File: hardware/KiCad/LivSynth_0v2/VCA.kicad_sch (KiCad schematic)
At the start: 24 parts, among them J18 Jumper, J6 Jumper, Q5 2N3904, Q6 2N3904, U3 TL074

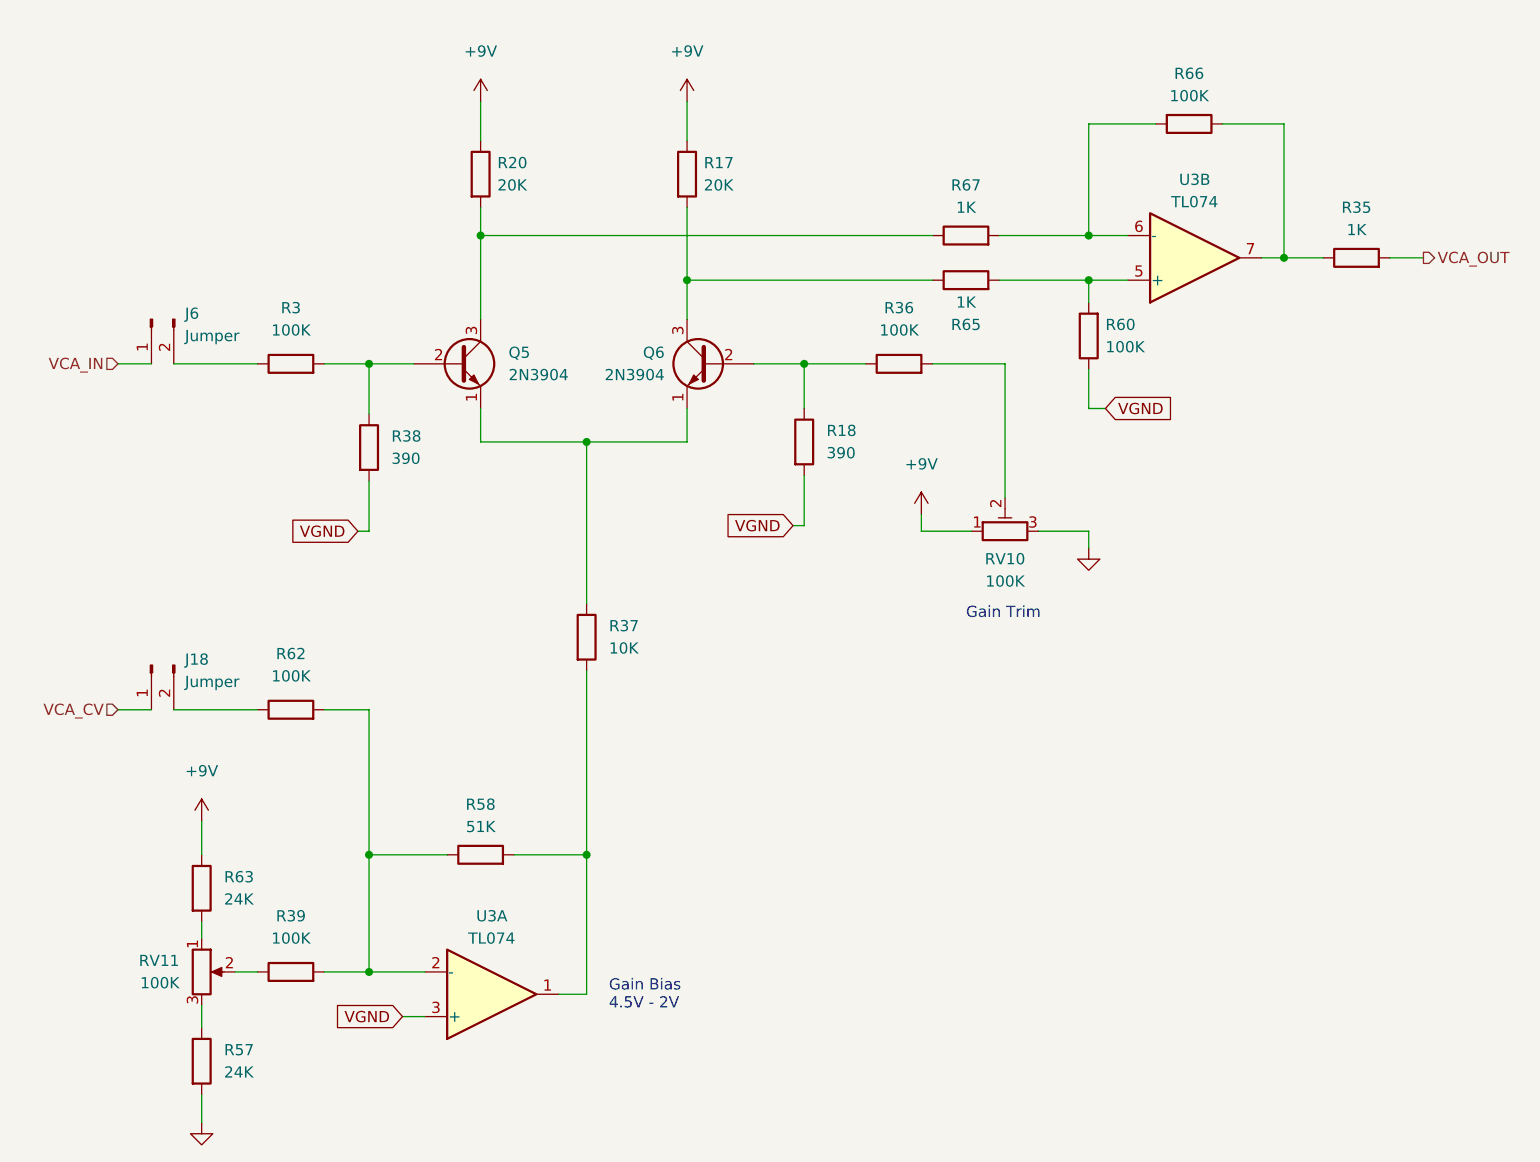
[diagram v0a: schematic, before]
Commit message: Analog redesign:  - Power: Add voltage and current test points  - MCU: use PA11/PA12 for USB DFU interface  - MCU: add NRST reset switch  - Slew: increase portamento cap  - VCO: invert trim pots  - VCF: let resonance kick in earlier  - VCF: invert pots  - VCA: invert trim pot  - EG: full redesign, properly referencing VGND now  - LFO: R61 = 51K  - ModMatrix: add EG attenuverters  - IO: invert pots  - IO: limit output gain for 1W speaker  - IO: connect BTN_SHIFT in gap free order to SR
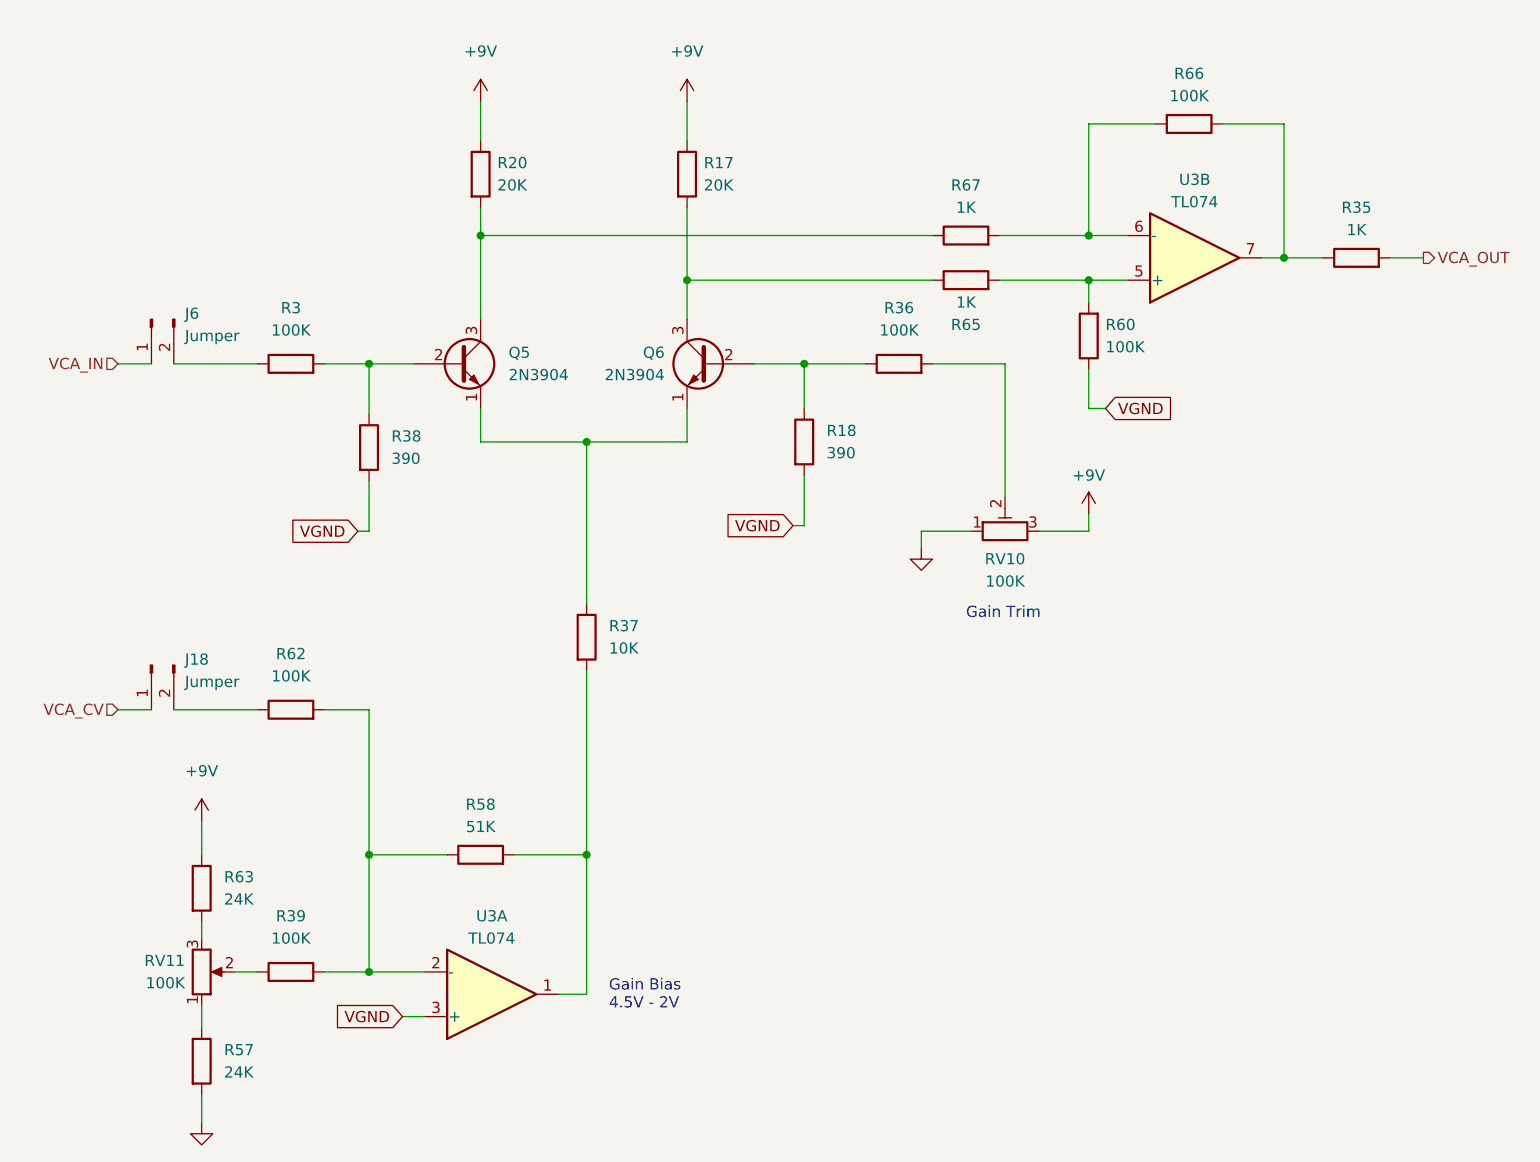
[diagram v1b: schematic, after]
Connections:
- net +9V: now also RV10.3; no longer RV10.1
- net GND: now also RV10.1; no longer RV10.3
- net at R63.2: now also RV11.3; no longer RV11.1
- net at R57.1: now also RV11.1; no longer RV11.3
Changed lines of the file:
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@@
+    (stroke (width 0) (type default) (color 0 0 0 0))
+  )
+  (wire (pts (xy 177.8 95.25) (xy 177.8 97.155))
     (stroke (width 0) (type default) (color 0 0 0 0))
   )
@@
     (stroke (width 0) (type default) (color 0 0 0 0))
   )
-  (wire (pts (xy 158.75 95.25) (xy 158.75 97.155))
-    (stroke (width 0) (type default) (color 0 0 0 0))
-  )
   (wire (pts (xy 95.885 78.105) (xy 100.965 78.105))
     (stroke (width 0) (type default) (color 0 0 0 0))
@@
     (stroke (width 0) (type default) (color 0 0 0 0))
   )
-  (wire (pts (xy 177.8 97.155) (xy 177.8 99.06))
+  (wire (pts (xy 158.75 97.155) (xy 158.75 99.06))
     (stroke (width 0) (type default) (color 0 0 0 0))
   )
@@
     (pin "2")
   )
-  (symbol (lib_id "Device:R_Potentiometer") (at 76.835 147.32 0) (unit 1)
-    (in_bom yes) (on_board yes) (fields_autoplaced)
-    (property "Reference" "RV11" (id 0) (at 74.295 146.0499 0)
-      (effects (font (size 1.27 1.27)) (justify right))
-    )
-    (property "Value" "100K" (id 1) (at 74.295 148.5899 0)
+  (symbol (lib_id "Device:R_Potentiometer") (at 76.835 147.32 0) (mirror x) (unit 1)
+    (in_bom yes) (on_board yes) (fields_autoplaced)
+    (property "Reference" "RV11" (id 0) (at 74.93 146.0499 0)
+      (effects (font (size 1.27 1.27)) (justify right))
+    )
+    (property "Value" "100K" (id 1) (at 74.93 148.5899 0)
       (effects (font (size 1.27 1.27)) (justify right))
     )
@@
     (pin "3")
   )
-  (symbol (lib_id "power:GND") (at 177.8 99.06 0) (unit 1)
-    (in_bom yes) (on_board yes) (fields_autoplaced)
-    (property "Reference" "#PWR059" (id 0) (at 177.8 105.41 0)
-      (effects (font (size 1.27 1.27)) hide)
-    )
-    (property "Value" "GND" (id 1) (at 177.8 104.14 0)
-      (effects (font (size 1.27 1.27)) hide)
-    )
-    (property "Footprint" "" (id 2) (at 177.8 99.06 0)
-      (effects (font (size 1.27 1.27)) hide)
-    )
-    (property "Datasheet" "" (id 3) (at 177.8 99.06 0)
+  (symbol (lib_id "power:GND") (at 158.75 99.06 0) (unit 1)
+    (in_bom yes) (on_board yes) (fields_autoplaced)
+    (property "Reference" "#PWR059" (id 0) (at 158.75 105.41 0)
+      (effects (font (size 1.27 1.27)) hide)
+    )
+    (property "Value" "GND" (id 1) (at 158.75 104.14 0)
+      (effects (font (size 1.27 1.27)) hide)
+    )
+    (property "Footprint" "" (id 2) (at 158.75 99.06 0)
+      (effects (font (size 1.27 1.27)) hide)
+    )
+    (property "Datasheet" "" (id 3) (at 158.75 99.06 0)
       (effects (font (size 1.27 1.27)) hide)
     )
@@
     (pin "2")
   )
-  (symbol (lib_id "power:+9V") (at 158.75 95.25 0) (unit 1)
-    (in_bom yes) (on_board yes) (fields_autoplaced)
-    (property "Reference" "#PWR058" (id 0) (at 158.75 99.06 0)
-      (effects (font (size 1.27 1.27)) hide)
-    )
-    (property "Value" "+9V" (id 1) (at 158.75 89.535 0))
-    (property "Footprint" "" (id 2) (at 158.75 95.25 0)
-      (effects (font (size 1.27 1.27)) hide)
-    )
-    (property "Datasheet" "" (id 3) (at 158.75 95.25 0)
-      (effects (font (size 1.27 1.27)) hide)
-    )
+  (symbol (lib_id "power:+9V") (at 177.8 95.25 0) (unit 1)
+    (in_bom yes) (on_board yes)
+    (property "Reference" "#PWR058" (id 0) (at 177.8 99.06 0)
+      (effects (font (size 1.27 1.27)) hide)
+    )
+    (property "Value" "+9V" (id 1) (at 177.8 90.805 0))
+    (property "Footprint" "" (id 2) (at 177.8 95.25 0)
+      (effects (font (size 1.27 1.27)) hide)
+    )
+    (property "Datasheet" "" (id 3) (at 177.8 95.25 0)
+      (effects (font (size 1.27 1.27)) hide)
+    )

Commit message: Analog Redesign:  - Power: Build ververse polarity protection using P-Mosfet and Zener Diode      - (https://www.youtube.com/watch?v=Ltx4vovY5Z4 - 1:28)  - Power: Build adjustable buck regulator for 8-9V stable voltage source  - PCB: Add location for order number ("JLCJLCJLCJLC")  - General: Add Tooling Holes for PCB assembly  - PCB: check frontend component layout for symmetry  - VCF: fix sound issues  - PCB: Add SloBlo icon  - PCB: Add switch labels to front side  - EG: test new design  - MCU: Add some debug pins
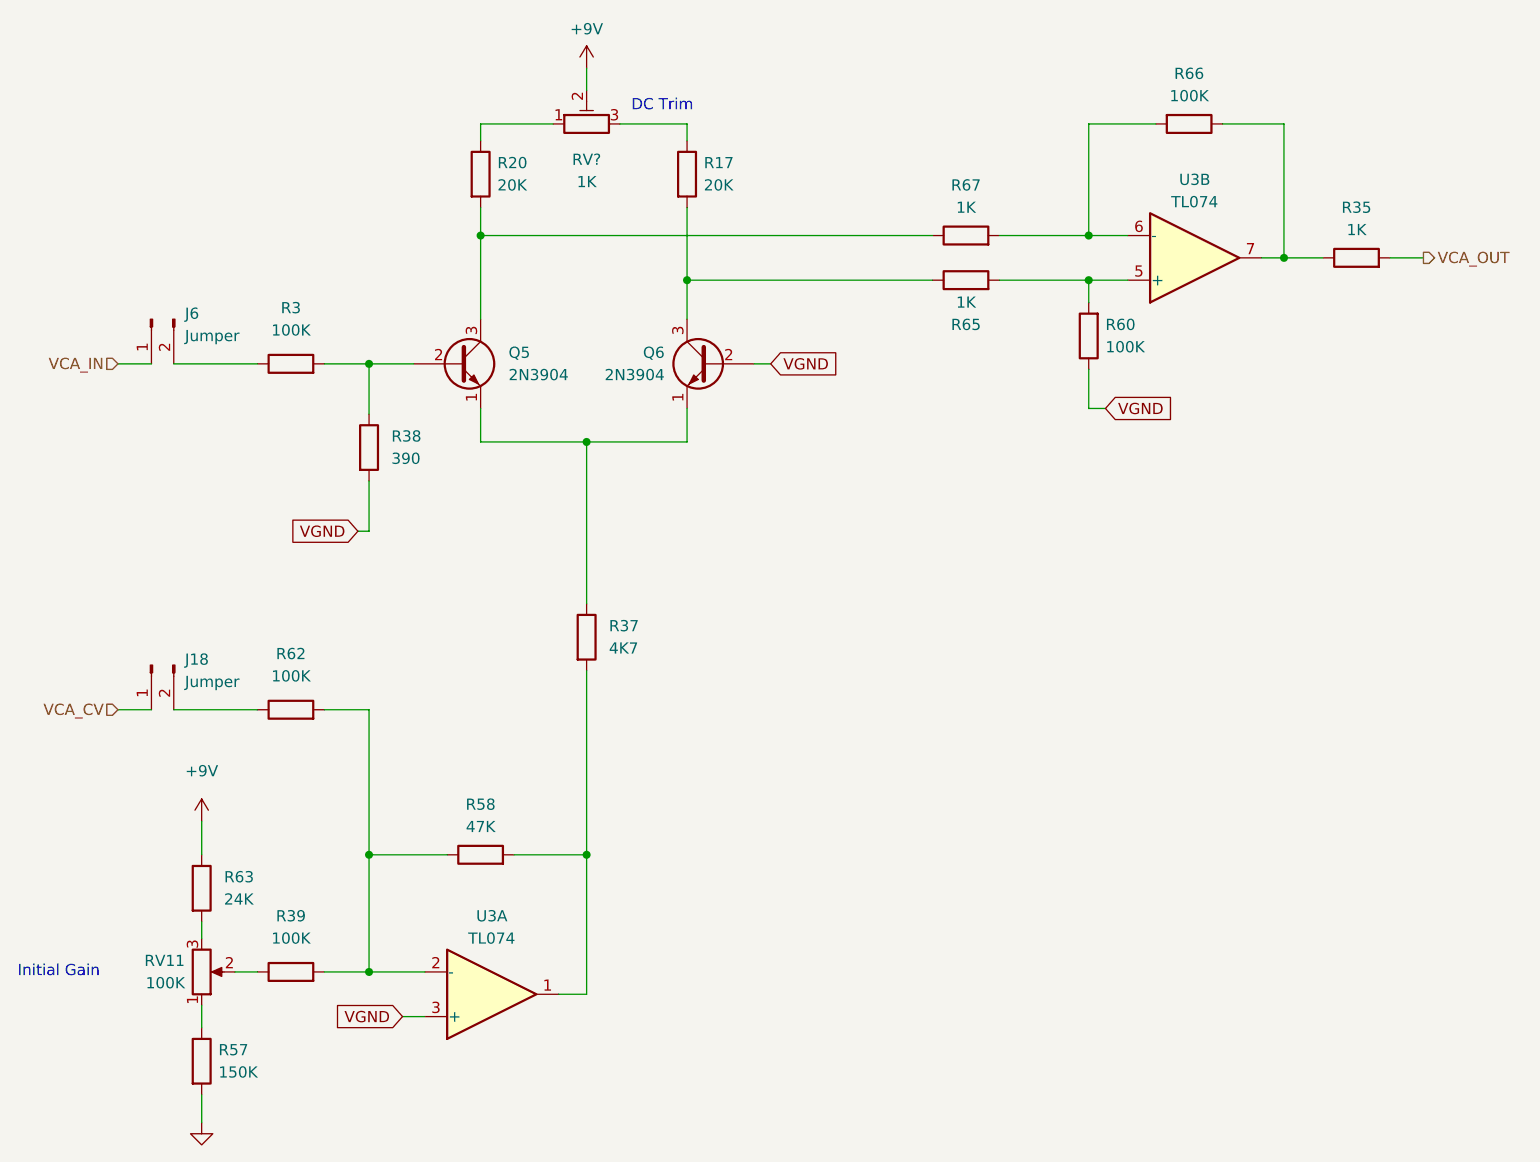
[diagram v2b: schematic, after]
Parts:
- removed R18: 390, Resistor_THT:R_Axial_DIN0207_L6.3mm_D2.5mm_P7.62mm_Horizontal, symbol Device:R
- removed R36: 100K, Resistor_THT:R_Axial_DIN0207_L6.3mm_D2.5mm_P7.62mm_Horizontal, symbol Device:R
- removed RV10: 100K, SloBlo:Potentiometer_Bourns_3296W_Vertical, symbol Device:R_Potentiometer_Trim
- added RV?: 1K, SloBlo:Potentiometer_Bourns_3296W_Vertical, symbol Device:R_Potentiometer_Trim
- R37: value 10K -> 4K7
- R57: value 24K -> 150K
- R58: value 51K -> 47K
- U3: LCSC (none) -> C2057504
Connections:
- net +9V: now also RV?.2; no longer R17.1, R20.1
- net VGND: now also Q6.2 (B)
- new net: R17.1, RV?.3
- new net: R20.1, RV?.1
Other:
- note added: "DC Trim"
- note added: "Initial Gain"
- note removed: "Gain Bias 4.5V - 2V"
- note removed: "Gain Trim"

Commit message: progress 2023-01-21
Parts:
- gave numbers to parts that had none: 1
- renumbered U3 to U1
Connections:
- net VGND: now also U1.10 (+); no longer U1.3 (+)
- net at R37.2, R58.2: now also U1.8; no longer U1.1
- net at R39.2, R58.1, R62.2: now also U1.9 (-); no longer U1.2 (-)
- net at R60.2, R65.2: now also U1.12 (+); no longer U1.5 (+)
- net at R66.2, R67.2: now also U1.13 (-); no longer U1.6 (-)
- net at R35.1, R66.1: now also U1.14; no longer U1.7
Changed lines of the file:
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@@
   (symbol (lib_id "Device:R_Potentiometer_Trim") (at 120.65 50.8 90) (unit 1)
     (in_bom yes) (on_board yes) (fields_autoplaced)
-    (property "Reference" "RV?" (id 0) (at 120.65 54.864 90))
+    (property "Reference" "RV1001" (id 0) (at 120.65 54.864 90))
     (property "Value" "1K" (id 1) (at 120.65 57.404 90))
     (property "Footprint" "SloBlo:Potentiometer_Bourns_3296W_Vertical" (id 2) (at 120.65 50.8 0)
@@
     (pin "3")
   )
-  (symbol (lib_id "Amplifier_Operational:TL074") (at 189.865 66.04 0) (mirror x) (unit 2)
-    (in_bom yes) (on_board yes)
-    (property "Reference" "U3" (id 0) (at 189.865 57.15 0))
+  (symbol (lib_id "Amplifier_Operational:TL074") (at 189.865 66.04 0) (mirror x) (unit 4)
+    (in_bom yes) (on_board yes)
+    (property "Reference" "U1" (id 0) (at 189.865 57.15 0))
     (property "Value" "TL074" (id 1) (at 189.865 59.69 0))
     (property "Footprint" "Package_SO:SOIC-14_3.9x8.7mm_P1.27mm" (id 2) (at 188.595 68.58 0)
@@
     (pin "2")
   )
-  (symbol (lib_id "Amplifier_Operational:TL074") (at 109.855 149.86 0) (mirror x) (unit 1)
-    (in_bom yes) (on_board yes)
-    (property "Reference" "U3" (id 0) (at 109.855 140.97 0))
+  (symbol (lib_id "Amplifier_Operational:TL074") (at 109.855 149.86 0) (mirror x) (unit 3)
+    (in_bom yes) (on_board yes)
+    (property "Reference" "U1" (id 0) (at 109.855 140.97 0))
     (property "Value" "TL074" (id 1) (at 109.855 143.51 0))
     (property "Footprint" "Package_SO:SOIC-14_3.9x8.7mm_P1.27mm" (id 2) (at 108.585 152.4 0)
